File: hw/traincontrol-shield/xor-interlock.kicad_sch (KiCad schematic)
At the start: 4 parts, among them U3 74LVC1G86, U4 74LVC2G08

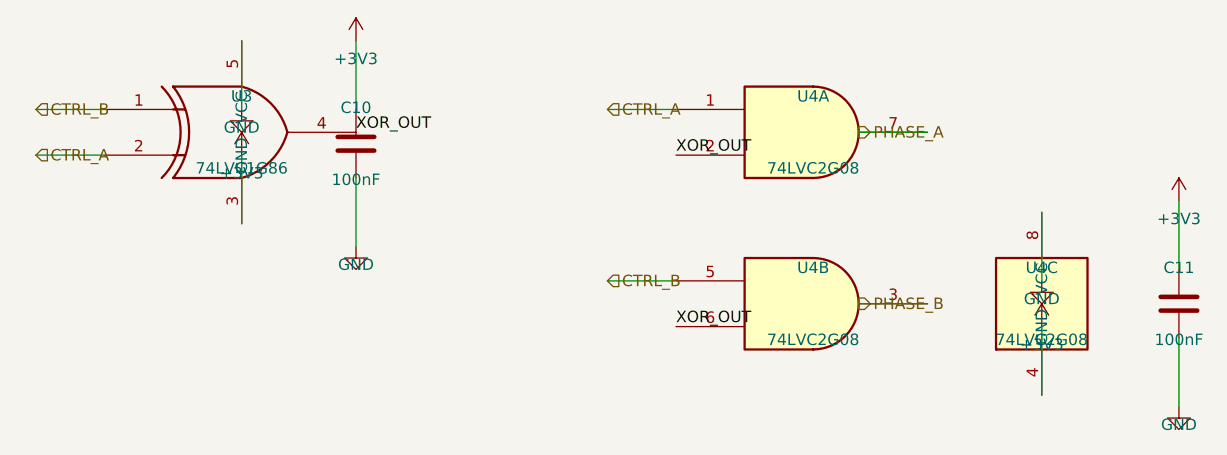
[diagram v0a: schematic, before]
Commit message: Fix hierarchical label placement and orientation in sub-sheets
Root cause: hlabel() placed the label at lx (stub tip) instead of x
(circuit connection point), mirroring the Issue-2 glabel bug fixed in
commit 2270223.

Fix applied to hlabel():
  (at {lx} ...) → (at {x} ...)  — label now sits at the circuit endpoint

Angle convention (matches label body direction):
  angle=180 → body extends LEFT  — left-side input/bidirectional labels
  angle=0   → body extends RIGHT — right-side output/bidirectional labels

Sheets affected: zero-crossing, xor-interlock, opto-triac-drive,
rail-voltage-sense; triacs-snubbers and mcu already had correct angles.

Co-Authored-By: Claude Sonnet 4.6 <noreply@anthropic.com>
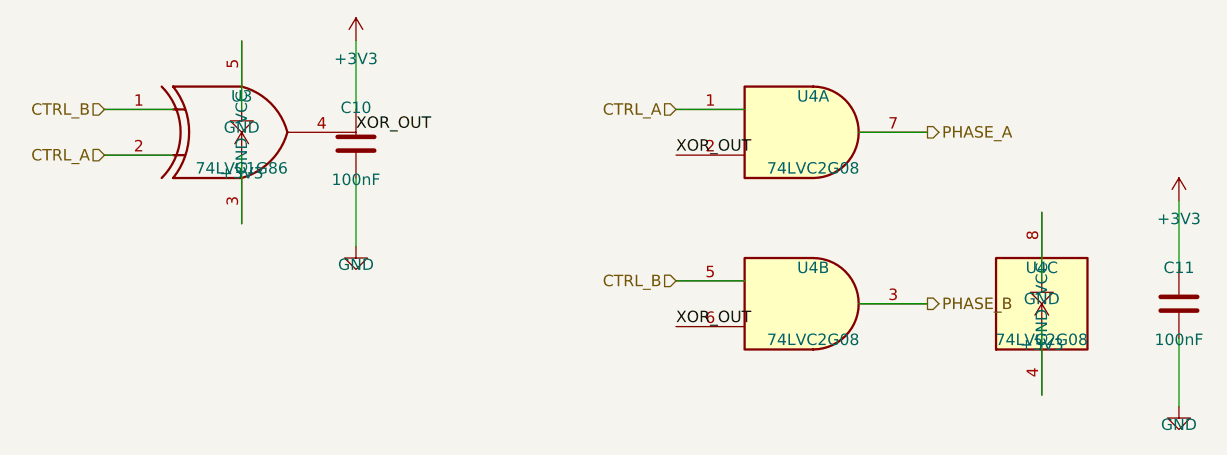
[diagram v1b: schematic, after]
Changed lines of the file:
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@@
 	)
 	(wire
-		(pts (xy 40.64 92.71) (xy 48.26 92.71))
+		(pts (xy 48.26 92.71) (xy 55.879999999999995 92.71))
 		(stroke (width 0) (type solid))
 	)
 	(hierarchical_label "CTRL_A"
 		(shape input)
-		(at 40.64 92.71 0)
+		(at 48.26 92.71 180)
 		(fields_autoplaced yes)
-		(effects (font (size 1.27 1.27)) (justify left bottom))
+		(effects (font (size 1.27 1.27)) (justify right bottom))
 		(property "Intersheetrefs" "${INTERSHEET_REFS}"
-			(at 40.64 92.71 0)
+			(at 48.26 92.71 0)
 			(effects (font (size 1.27 1.27)) (hide yes))
 		)
 	)
 	(wire
-		(pts (xy 40.64 87.63) (xy 48.26 87.63))
+		(pts (xy 48.26 87.63) (xy 55.879999999999995 87.63))
 		(stroke (width 0) (type solid))
 	)
 	(hierarchical_label "CTRL_B"
 		(shape input)
-		(at 40.64 87.63 0)
+		(at 48.26 87.63 180)
 		(fields_autoplaced yes)
-		(effects (font (size 1.27 1.27)) (justify left bottom))
+		(effects (font (size 1.27 1.27)) (justify right bottom))
 		(property "Intersheetrefs" "${INTERSHEET_REFS}"
-			(at 40.64 87.63 0)
+			(at 48.26 87.63 0)
 			(effects (font (size 1.27 1.27)) (hide yes))
 		)
@@
 	)
 	(wire
-		(pts (xy 104.14 87.63) (xy 111.76 87.63))
+		(pts (xy 111.76 87.63) (xy 119.38000000000001 87.63))
 		(stroke (width 0) (type solid))
 	)
 	(hierarchical_label "CTRL_A"
 		(shape input)
-		(at 104.14 87.63 0)
+		(at 111.76 87.63 180)
 		(fields_autoplaced yes)
-		(effects (font (size 1.27 1.27)) (justify left bottom))
+		(effects (font (size 1.27 1.27)) (justify right bottom))
 		(property "Intersheetrefs" "${INTERSHEET_REFS}"
-			(at 104.14 87.63 0)
+			(at 111.76 87.63 0)
 			(effects (font (size 1.27 1.27)) (hide yes))
 		)
 	)
 	(wire
-		(pts (xy 104.14 106.68) (xy 111.76 106.68))
+		(pts (xy 111.76 106.68) (xy 119.38000000000001 106.68))
 		(stroke (width 0) (type solid))
 	)
 	(hierarchical_label "CTRL_B"
 		(shape input)
-		(at 104.14 106.68 0)
+		(at 111.76 106.68 180)
 		(fields_autoplaced yes)
-		(effects (font (size 1.27 1.27)) (justify left bottom))
+		(effects (font (size 1.27 1.27)) (justify right bottom))
 		(property "Intersheetrefs" "${INTERSHEET_REFS}"
-			(at 104.14 106.68 0)
+			(at 111.76 106.68 0)
 			(effects (font (size 1.27 1.27)) (hide yes))
 		)
@@
 	(hierarchical_label "PHASE_A"
 		(shape output)
-		(at 132.07999999999998 90.17 0)
+		(at 139.7 90.17 0)
 		(fields_autoplaced yes)
 		(effects (font (size 1.27 1.27)) (justify left bottom))
 		(property "Intersheetrefs" "${INTERSHEET_REFS}"
-			(at 132.07999999999998 90.17 0)
+			(at 139.7 90.17 0)
 			(effects (font (size 1.27 1.27)) (hide yes))
 		)
@@
 	(hierarchical_label "PHASE_B"
 		(shape output)
-		(at 132.07999999999998 109.22 0)
+		(at 139.7 109.22 0)
 		(fields_autoplaced yes)
 		(effects (font (size 1.27 1.27)) (justify left bottom))
 		(property "Intersheetrefs" "${INTERSHEET_REFS}"
-			(at 132.07999999999998 109.22 0)
+			(at 139.7 109.22 0)
 			(effects (font (size 1.27 1.27)) (hide yes))
 		)
